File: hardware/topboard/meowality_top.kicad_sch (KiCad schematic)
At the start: 0 parts

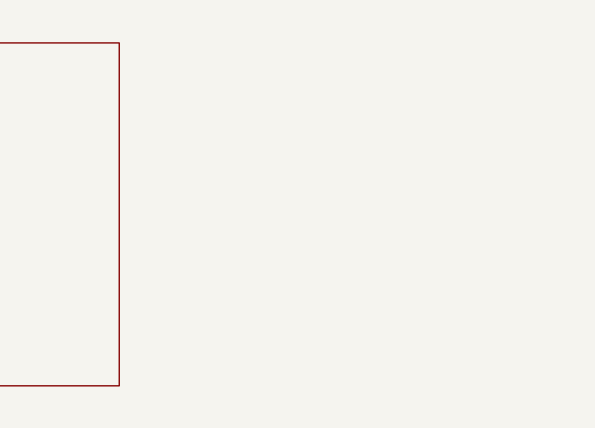
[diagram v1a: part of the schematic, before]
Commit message: Add basic power rails
Signed-off-by: gatecat <gatecat@ds0.me>
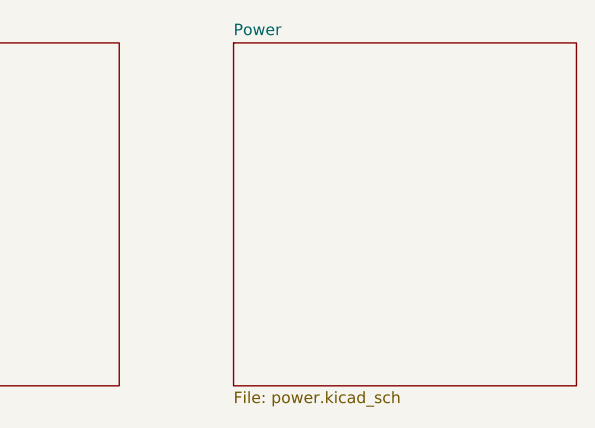
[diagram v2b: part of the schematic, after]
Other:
- added sheet Power (power.kicad_sch)

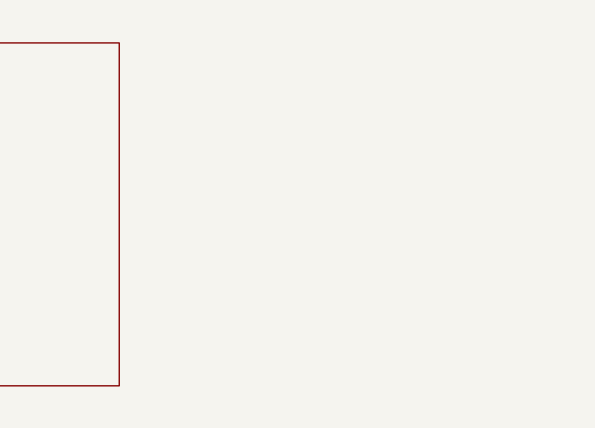
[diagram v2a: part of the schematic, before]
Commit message: Add microdisplay and its power supply
Signed-off-by: gatecat <gatecat@ds0.me>
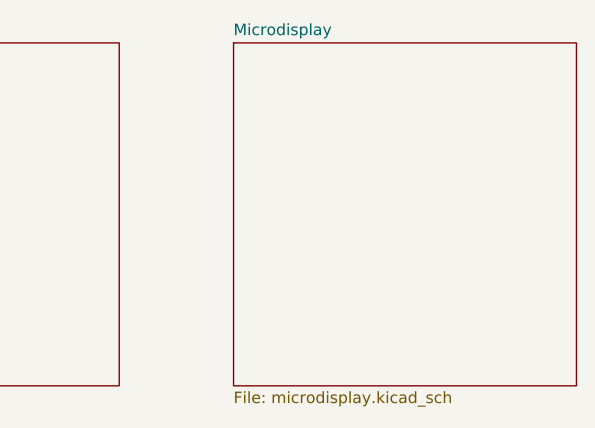
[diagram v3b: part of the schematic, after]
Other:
- added sheet Microdisplay (microdisplay.kicad_sch)

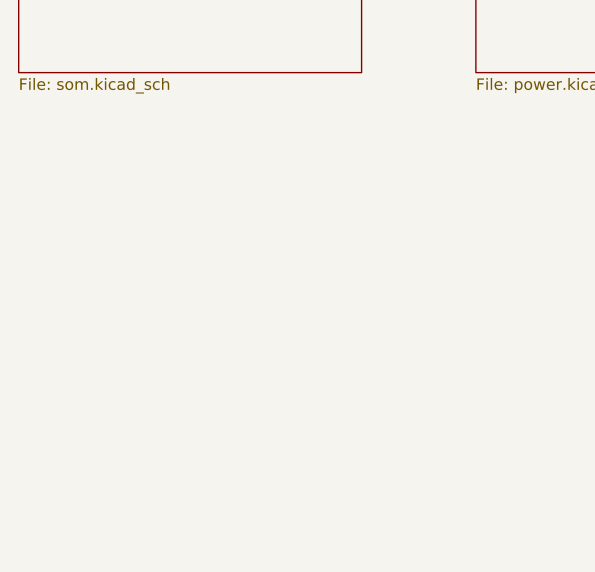
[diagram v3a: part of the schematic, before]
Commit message: Pin planning the main b2b connectors
Signed-off-by: gatecat <gatecat@ds0.me>
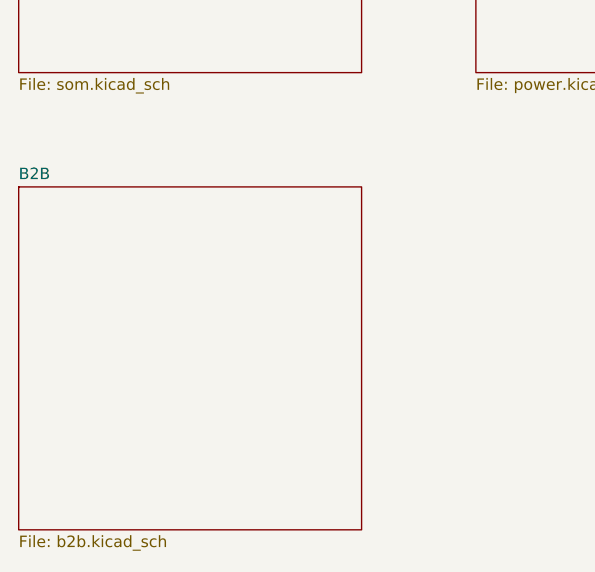
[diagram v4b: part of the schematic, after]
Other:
- added sheet B2B (b2b.kicad_sch)

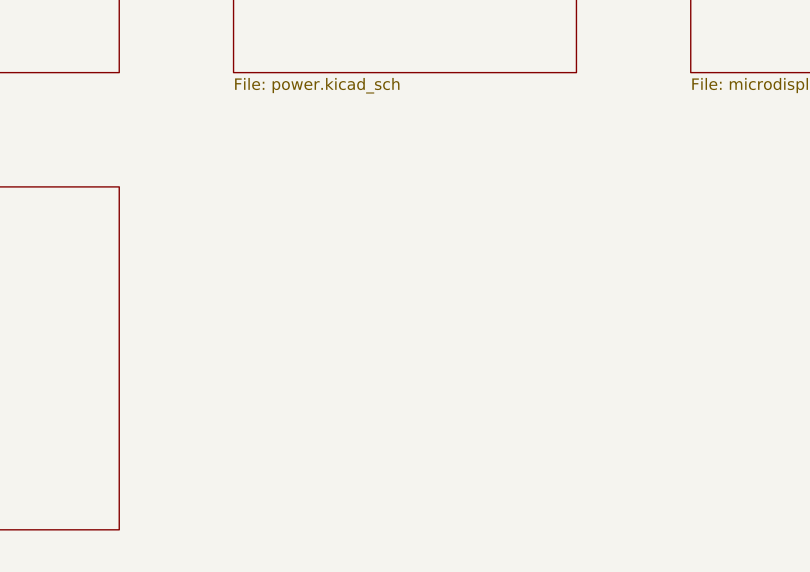
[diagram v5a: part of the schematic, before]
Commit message: SD card, ULPI PHY, JTAG/UART
Signed-off-by: gatecat <gatecat@ds0.me>
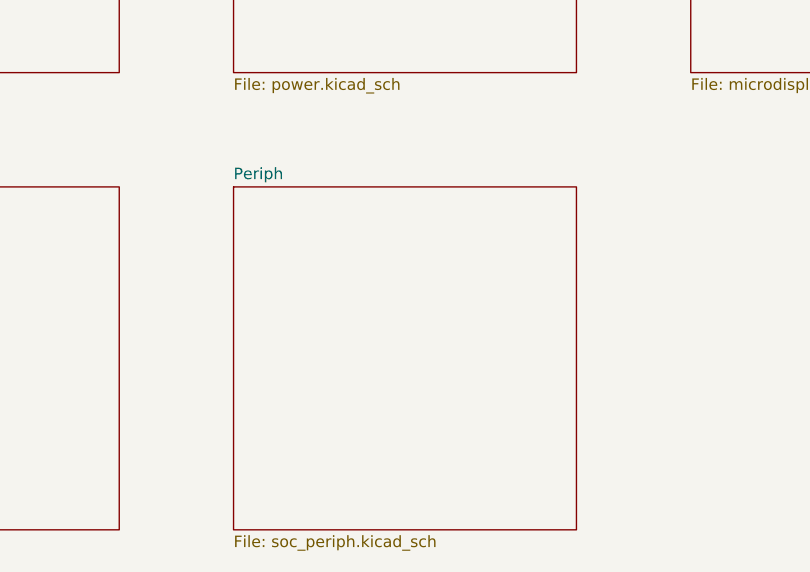
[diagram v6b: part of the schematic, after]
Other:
- added sheet Periph (soc_periph.kicad_sch)
